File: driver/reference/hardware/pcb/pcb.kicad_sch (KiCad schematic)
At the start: 26 parts, among them J1 Screw_Terminal_01x02, U1 AMS1117-3.3, U2 AK09911C, U3 MAX13487EESA

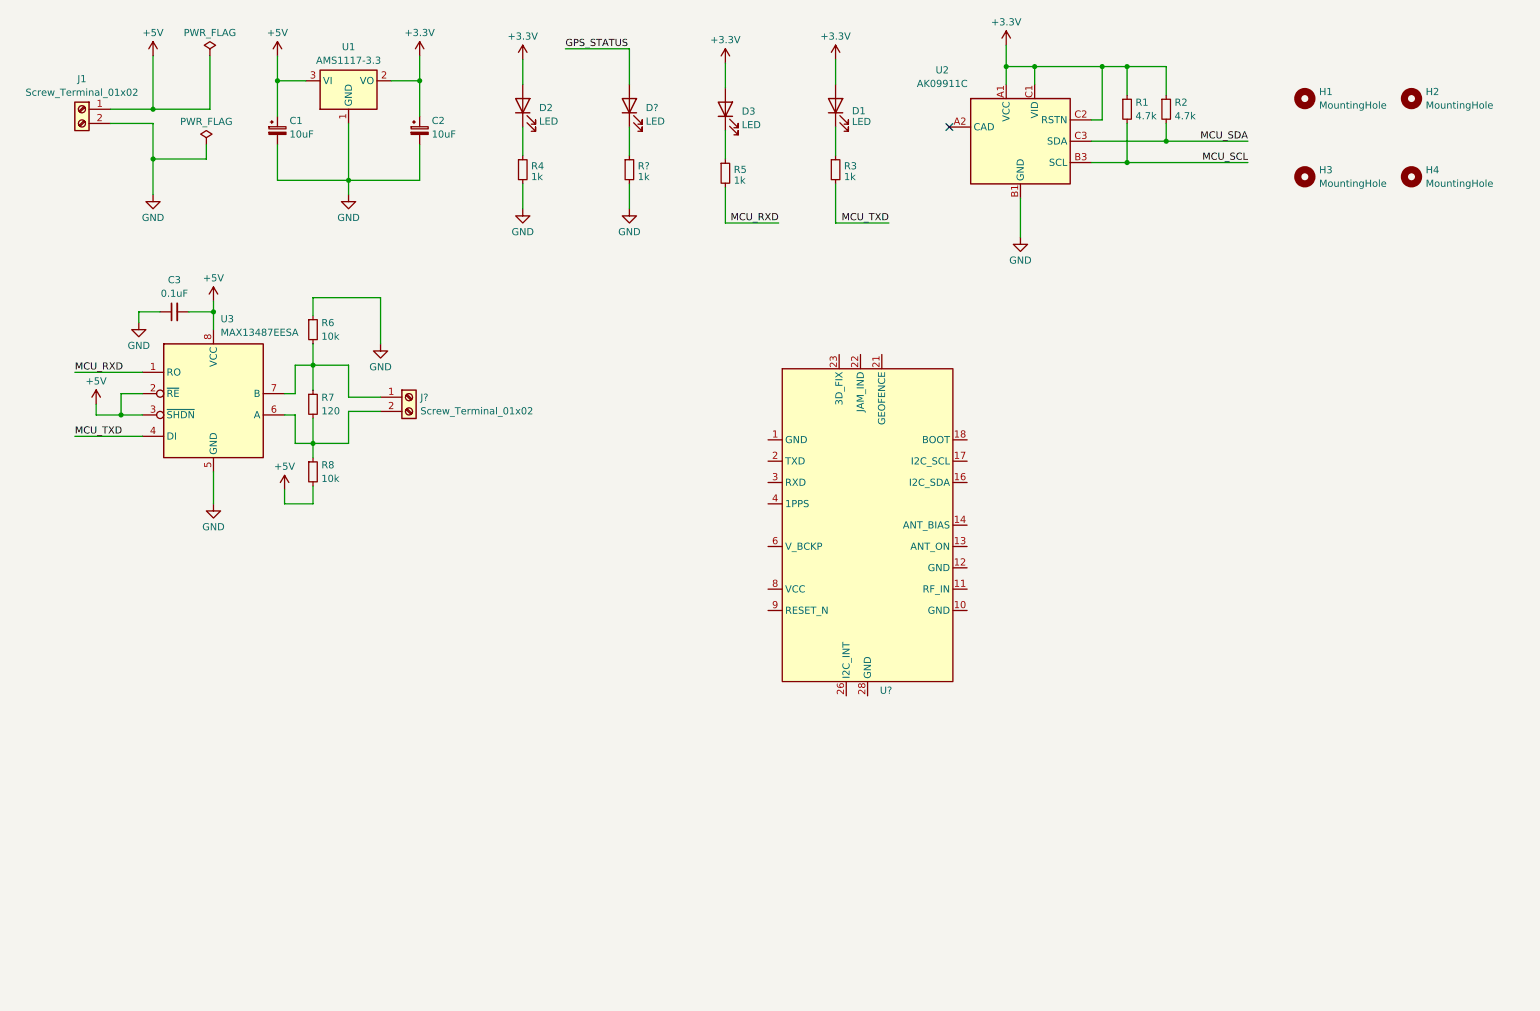
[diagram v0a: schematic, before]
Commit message: Basic implementation of frontend
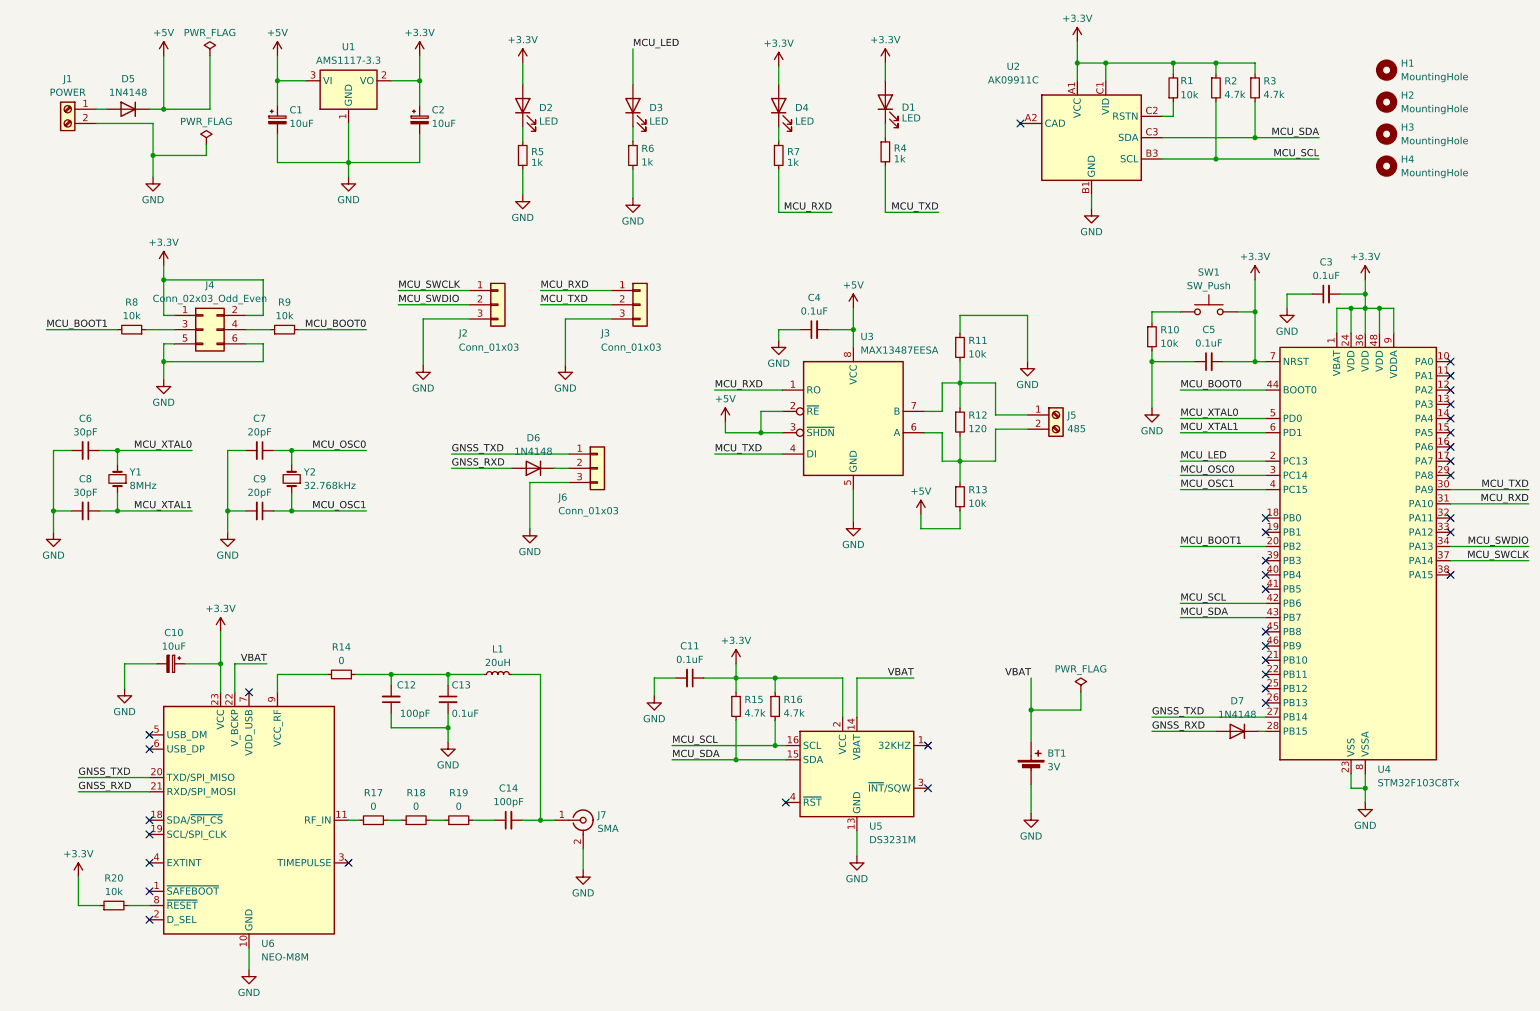
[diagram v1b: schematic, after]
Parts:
- removed D?: LED, LED_THT:LED_D3.0mm, symbol Device:LED
- removed R?: 1k, Resistor_THT:R_Axial_DIN0204_L3.6mm_D1.6mm_P7.62mm_Horizontal, symbol Device:R_Small
- removed U?: ~, OpenStation:LC760Z, symbol OpenStation:LC760Z
- added BT1: 3V, Battery:BatteryHolder_LINX_BAT-HLD-012-SMT, symbol Device:Battery_Cell
- added C10: 10uF, Capacitor_THT:CP_Radial_D5.0mm_P2.50mm, symbol Device:C_Polarized_Small
- added C11, C13, C3, C5: 0.1uF, Capacitor_THT:C_Disc_D3.0mm_W2.0mm_P2.50mm, symbol Device:C_Small
- added C12, C14: 100pF, Capacitor_THT:C_Disc_D3.0mm_W2.0mm_P2.50mm, symbol Device:C_Small
- added C6, C8: 30pF, Capacitor_THT:C_Disc_D3.0mm_W2.0mm_P2.50mm, symbol Device:C_Small
- added C7, C9: 20pF, Capacitor_THT:C_Disc_D3.0mm_W2.0mm_P2.50mm, symbol Device:C_Small
- added D3: LED, LED_THT:LED_D3.0mm, symbol Device:LED
- added D5, D6, D7: 1N4148, Diode_THT:D_DO-35_SOD27_P7.62mm_Horizontal, symbol Diode:1N4148
- added J2, J3, J6: Conn_01x03, Connector_PinHeader_2.54mm:PinHeader_1x03_P2.54mm_Vertical, symbol Connector_Generic:Conn_01x03
- added J4: Conn_02x03_Odd_Even, Connector_PinHeader_2.54mm:PinHeader_2x03_P2.54mm_Vertical, symbol Connector_Generic:Conn_02x03_Odd_Even
- added J7: SMA, Connector_Coaxial:SMA_Amphenol_901-144_Vertical, symbol Connector:Conn_Coaxial
- added L1: 20uH, Inductor_THT:L_Radial_D7.0mm_P3.00mm, symbol Device:L_Small
- added R1, R10, R20, R8, R9: 10k, Resistor_THT:R_Axial_DIN0204_L3.6mm_D1.6mm_P7.62mm_Horizontal, symbol Device:R_Small
- added R14, R17, R18, R19: 0, Resistor_THT:R_Axial_DIN0204_L3.6mm_D1.6mm_P7.62mm_Horizontal, symbol Device:R_Small
- added R15, R16: 4.7k, Resistor_THT:R_Axial_DIN0204_L3.6mm_D1.6mm_P7.62mm_Horizontal, symbol Device:R_Small
- added R6: 1k, Resistor_THT:R_Axial_DIN0204_L3.6mm_D1.6mm_P7.62mm_Horizontal, symbol Device:R_Small
- added SW1: SW_Push, Button_Switch_SMD:SW_SPST_FSMSM, symbol Switch:SW_Push
- added U4: STM32F103C8Tx, Package_QFP:LQFP-48_7x7mm_P0.5mm, symbol MCU_ST_STM32F1:STM32F103C8Tx
- added U5: DS3231M, Package_SO:SOIC-16W_7.5x10.3mm_P1.27mm, symbol Timer_RTC:DS3231M
- added U6: NEO-M8M, RF_GPS:ublox_NEO, symbol RF_GPS:NEO-M8M
- added Y1: 8MHz, Crystal:Crystal_HC18-U_Vertical, symbol Device:Crystal_Small
- added Y2: 32.768kHz, Crystal:Crystal_DS26_D2.0mm_L6.0mm_Horizontal, symbol Device:Crystal_Small
- C4: renamed from C3; footprint (none) -> Capacitor_THT:C_Disc_D3.0mm_W2.0mm_P2.50mm
- H1, H2, H3, H4: footprint MountingHole:MountingHole_3.2mm_M3 -> MountingHole:MountingHole_3.2mm_M3_DIN965
- J1: value Screw_Terminal_01x02 -> POWER; footprint (none) -> TerminalBlock:TerminalBlock_bornier-2_P5.08mm
- J5: renamed from J?; value Screw_Terminal_01x02 -> 485; footprint (none) -> TerminalBlock:TerminalBlock_bornier-2_P5.08mm
- R11: renamed from R6; footprint (none) -> Resistor_THT:R_Axial_DIN0204_L3.6mm_D1.6mm_P7.62mm_Horizontal
- R12: renamed from R7; footprint (none) -> Resistor_THT:R_Axial_DIN0204_L3.6mm_D1.6mm_P7.62mm_Horizontal
- R13: renamed from R8; footprint (none) -> Resistor_THT:R_Axial_DIN0204_L3.6mm_D1.6mm_P7.62mm_Horizontal
- R2: renamed from R1; footprint (none) -> Resistor_THT:R_Axial_DIN0204_L3.6mm_D1.6mm_P7.62mm_Horizontal
- R3: renamed from R2; footprint (none) -> Resistor_THT:R_Axial_DIN0204_L3.6mm_D1.6mm_P7.62mm_Horizontal
- renumbered D3 to D4, R3 to R4, R4 to R5, R5 to R7
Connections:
- net +3.3V: now also C10.1, C11.1, C3.2, C5.2, J4.1 (Pin_1), J4.2 (Pin_2), R1.2, R15.1, R16.1, R20.1, SW1.1, U4.1 (VBAT), U4.24 (VDD), U4.36 (VDD), U4.48 (VDD), U4.7 (NRST), U4.9 (VDDA), U5.2 (VCC), U6.23 (VCC); no longer U2.C2 (RSTN)
- net +5V: now also D5.1 (K); no longer J1.1 (Pin_1)
- net GND: now also BT1.2 (-), C10.2, C11.2, C12.1, C13.2, C3.1, C5.1, C6.2, C7.2, C8.2, C9.2, J2.3 (Pin_3), J3.3 (Pin_3), J4.5 (Pin_5), J4.6 (Pin_6), J6.3 (Pin_3), J7.2 (Ext), R10.2, R6.2, U4.23 (VSS), U4.35 (VSS), U4.47 (VSS), U4.8 (VSSA), U5.10 (GND), U5.11 (GND), U5.12 (GND), U5.13 (GND), U5.5 (GND), U5.6 (GND), U5.7 (GND), U5.8 (GND), U5.9 (GND), U6.10 (GND), U6.12 (GND), U6.13 (GND), U6.24 (GND)
- net MCU_RXD: now also J3.1 (Pin_1), U4.31 (PA10)
- net MCU_SCL: now also R16.2, U4.42 (PB6), U5.16 (SCL)
- net MCU_SDA: now also R15.2, U4.43 (PB7), U5.15 (SDA)
- net MCU_TXD: now also J3.2 (Pin_2), U4.30 (PA9)
- new net: D3.1 (K), R6.1
- new net: J4.3 (Pin_3), R8.1
- new net: J4.4 (Pin_4), R9.1
- new net: R17.1, R18.1
- new net: R17.2, U6.11 (RF_IN)
- new net: R20.2, U6.8 (~{RESET})
- new net: R14.2, U6.9 (VCC_RF)
- new net: R10.1, SW1.2
- new net: R1.1, U2.C2 (RSTN)
- new net: D7.1 (K), U4.28 (PB15)
- new net: C12.2, C13.1, L1.1, R14.1
- new net: C14.2, J7.1 (In), L1.2
- new net: R18.2, R19.1
- new net: C14.1, R19.2
- new net: D6.1 (K), J6.2 (Pin_2)
- new net: D5.2 (A), J1.1 (Pin_1)
- new net GNSS_RXD: D6.2 (A), D7.2 (A), U6.21 (RXD/SPI_MOSI)
- new net GNSS_TXD: J6.1 (Pin_1), U4.27 (PB14), U6.20 (TXD/SPI_MISO)
- new net MCU_BOOT0: R9.2, U4.44 (BOOT0)
- new net MCU_BOOT1: R8.2, U4.20 (PB2)
- new net MCU_LED: D3.2 (A), U4.2 (PC13)
- new net MCU_OSC0: C7.1, U4.3 (PC14), Y2.2
- new net MCU_OSC1: C9.1, U4.4 (PC15), Y2.1
- new net MCU_SWCLK: J2.1 (Pin_1), U4.37 (PA14)
- new net MCU_SWDIO: J2.2 (Pin_2), U4.34 (PA13)
- new net MCU_XTAL0: C6.1, U4.5 (PD0), Y1.2
- new net MCU_XTAL1: C8.1, U4.6 (PD1), Y1.1
- new net VBAT: BT1.1 (+), U5.14 (VBAT), U6.22 (V_BCKP)
- no-connect marks 1 -> 36
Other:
- moved on the sheet: C1, C2, C4, D1, D4, H1, H2, H3, H4, J1, J5, R11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

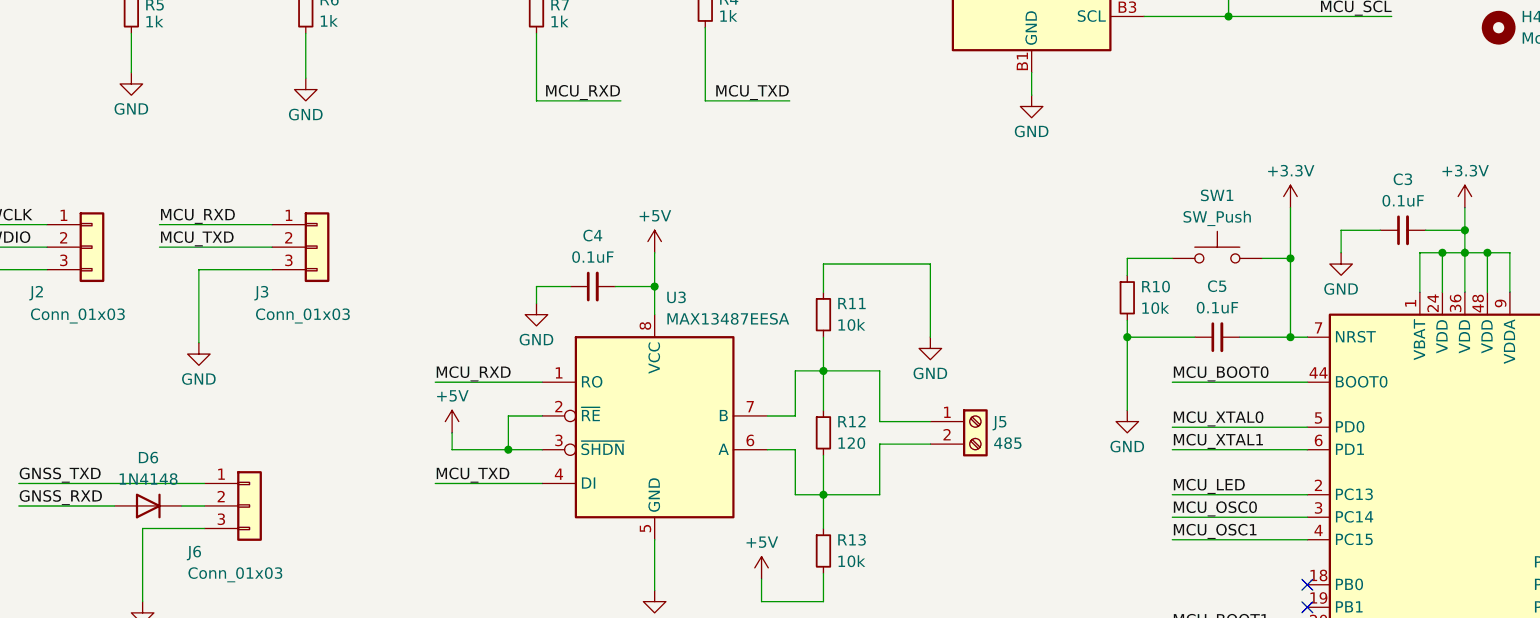
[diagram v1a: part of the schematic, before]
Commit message: Updated reference board schematic & firmware
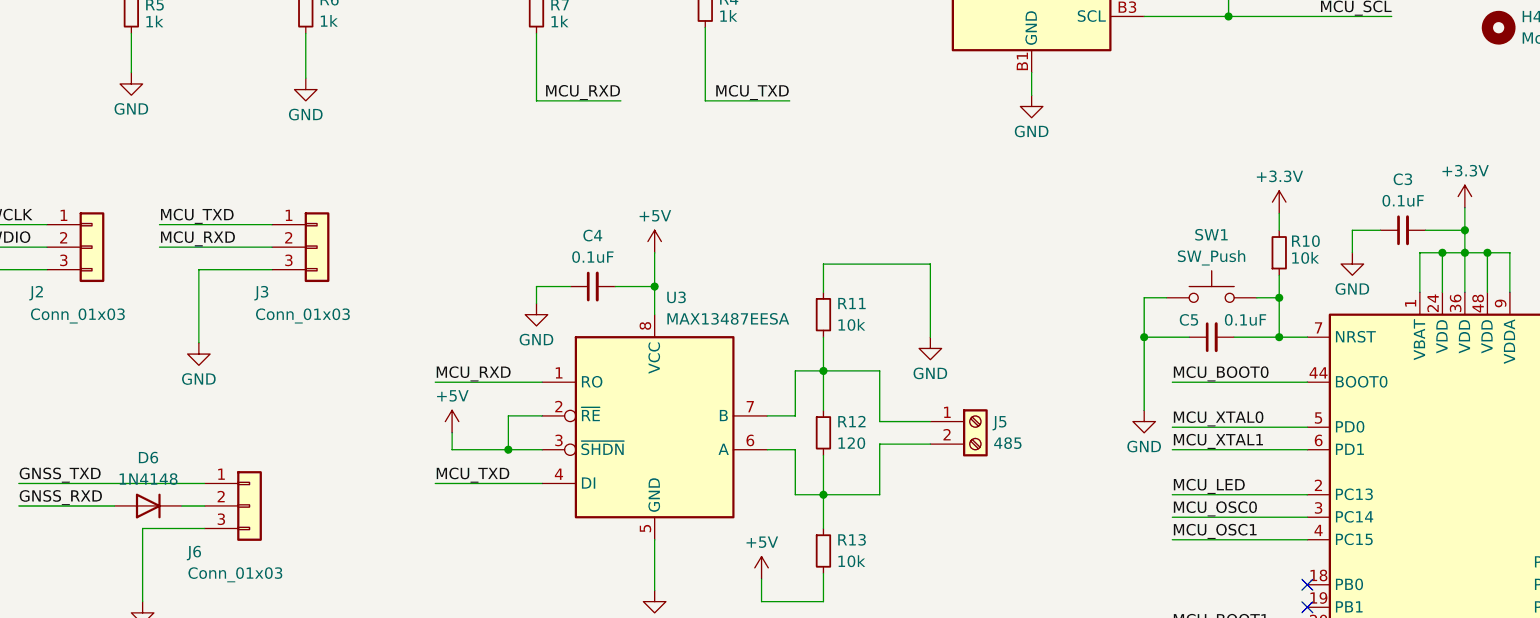
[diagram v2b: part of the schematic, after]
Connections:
- net +3.3V: now also R10.2; no longer C5.2, SW1.1, U4.7 (NRST)
- net GND: now also SW1.2; no longer R10.2
- net MCU_RXD: now also J3.2 (Pin_2); no longer J3.1 (Pin_1)
- net MCU_TXD: now also J3.1 (Pin_1); no longer J3.2 (Pin_2)
- net at R10.1: now also C5.2, SW1.1, U4.7 (NRST); no longer SW1.2
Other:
- moved on the sheet: C5, R10, SW1
